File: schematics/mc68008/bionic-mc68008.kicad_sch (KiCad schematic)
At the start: 11 parts, among them J1 Bionic-P135, J2 Bionic-P245, U1 MC68008P, U2 74HCT126, U3 74HCT541, U4 74HCT541, U5 11AA010-I/TO

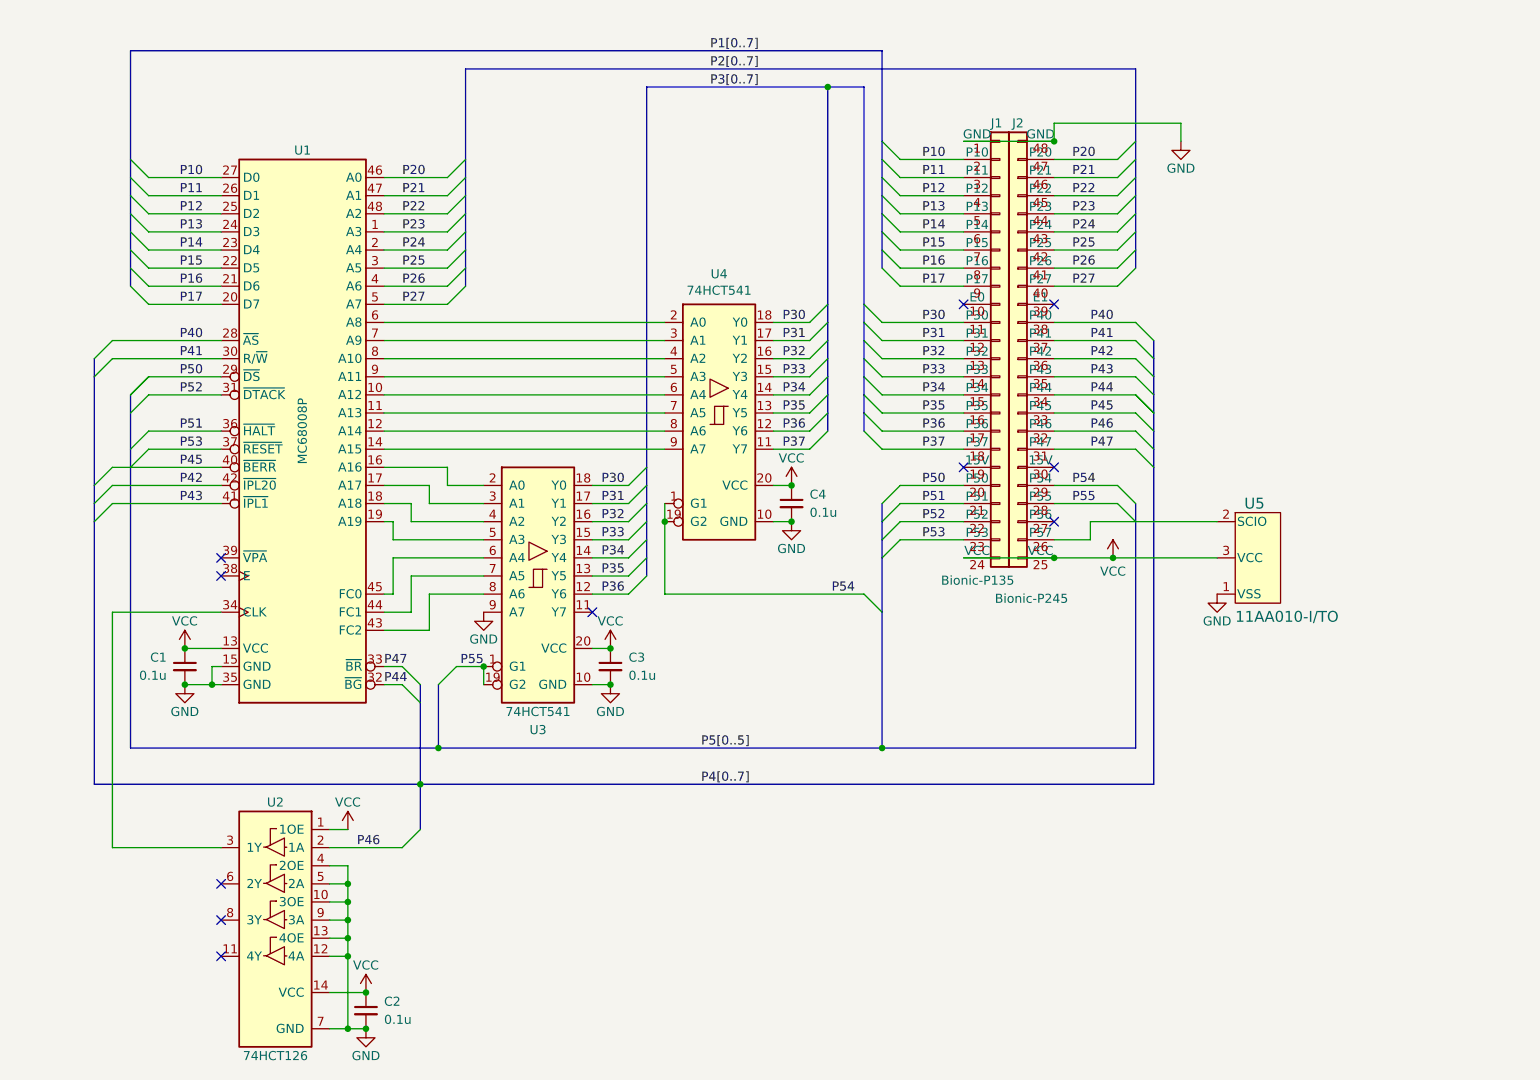
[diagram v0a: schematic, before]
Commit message: [WIP] [MC68008] Update schematics
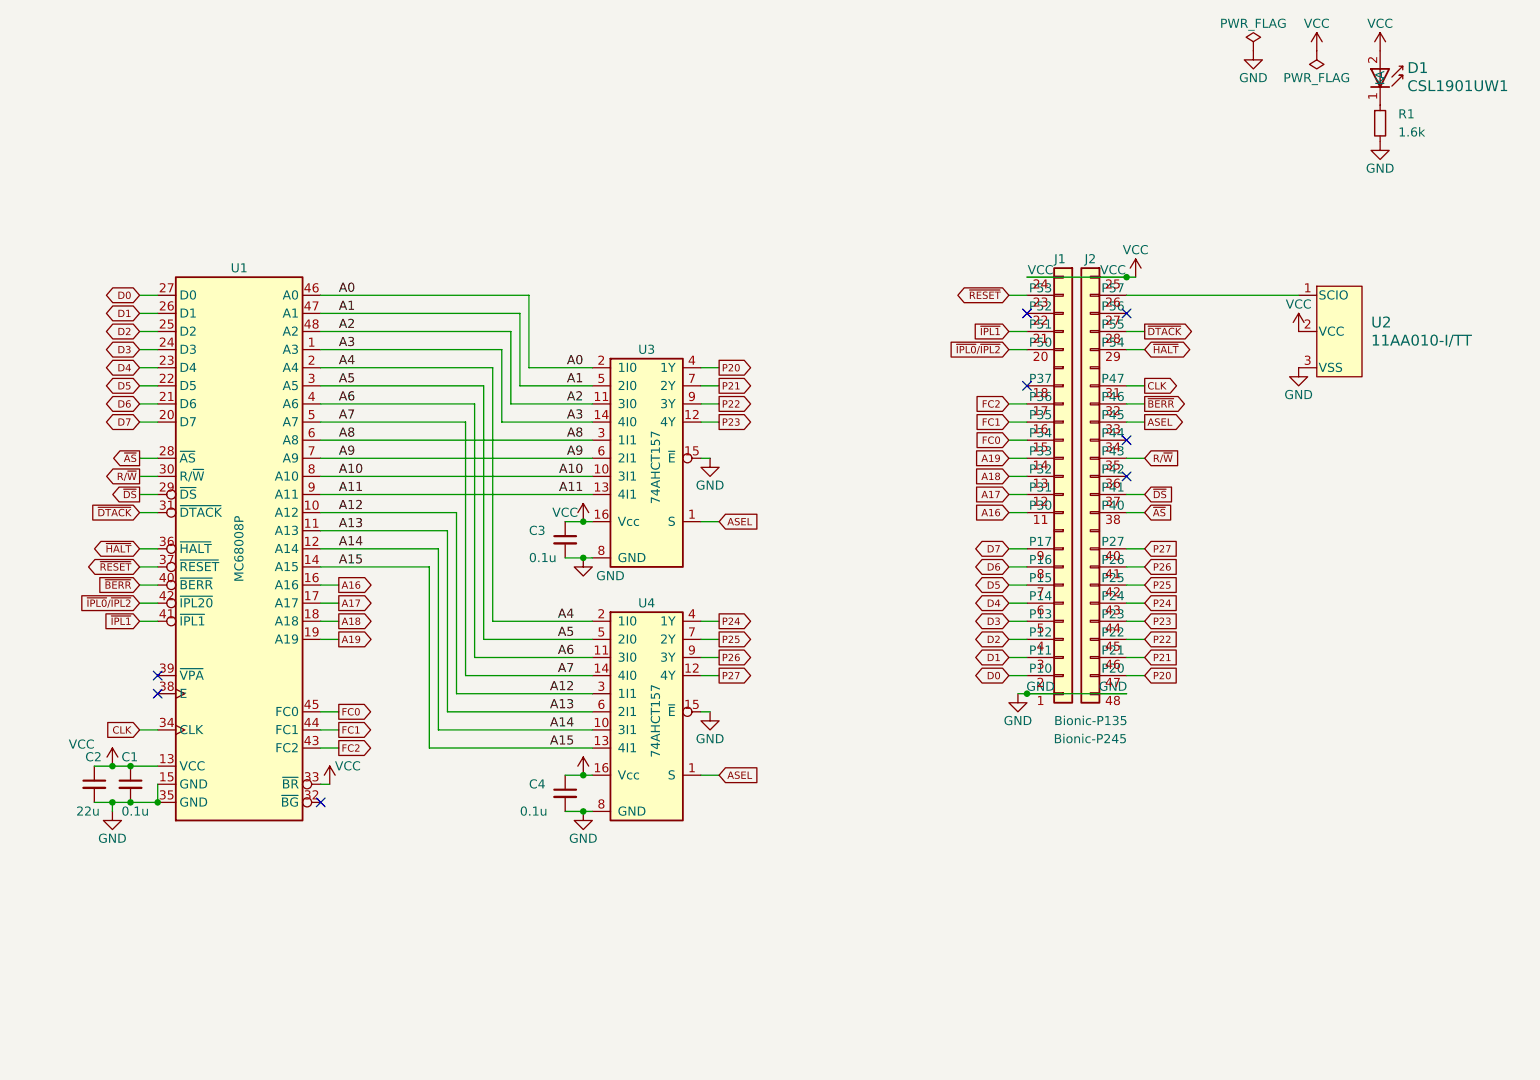
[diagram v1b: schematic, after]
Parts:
- removed J1: Bionic-P135, connector:Bionic-P135_Vertical, symbol 0-LocalLibrary:Bionic-P135
- removed J2: Bionic-P245, connector:Bionic-P245_Vertical, symbol 0-LocalLibrary:Bionic-P245
- removed U1: MC68008P, Package_DIP:DIP-48_W15.24mm, symbol 0-LocalLibrary:MC68008P
- removed U2: 74HCT126, Package_DIP:DIP-14_W7.62mm, symbol 0-LocalLibrary:74HCT126
- removed U3, U4: 74HCT541, Package_DIP:DIP-20_W7.62mm, symbol 0-LocalLibrary:74HCT541
- removed U5: 11AA010-I/TO, TO-92_MC_MCH, symbol 0-LocalLibrary:11AA010-I_TO
- added D1: CSL1901UW1, rhom:LED_CSL1901UW1_ROM-M, symbol rhom:CSL1901UW1
- added J1: Bionic-P135, bionic:Bionic-P135_SMT, symbol bionic:Bionic-P135
- added J2: Bionic-P245, bionic:Bionic-P245_SMT, symbol bionic:Bionic-P245
- added R1: 1.6k, Resistor_SMD:R_0603_1608Metric_Pad0.98x0.95mm_HandSolder, symbol Device:R_Small
- added U1: MC68008P, bionic:DIP-48_W15.24mm_Socket, symbol cpu:MC68008P
- added U2: 11AA010-I/TT, microchip:SOT-23_MC_MCH-M, symbol microchip:11AA010-I_TT
- added U3, U4: 74AHCT157, ti:PW16-M, symbol ti:74AHCT157
- C1, C3, C4: footprint Capacitor_THT:C_Disc_D3.4mm_W2.1mm_P2.50mm -> Capacitor_SMD:C_0603_1608Metric_Pad1.08x0.95mm_HandSolder
- C2: value 0.1u -> 22u; footprint Capacitor_THT:C_Disc_D3.4mm_W2.1mm_P2.50mm -> Capacitor_SMD:C_0603_1608Metric_Pad1.08x0.95mm_HandSolder
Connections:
- net GND: now also J1.1 (GND), J2.48 (GND), R1.2, U1.15 (GND), U1.35 (GND), U2.3 (VSS), U3.15 (~{E}), U3.8 (GND), U4.15 (~{E}), U4.8 (GND)
- net P20: now also J2.47 (P20), U3.4 (1Y)
- net P21: now also J2.46 (P21), U3.7 (2Y)
- net P22: now also J2.45 (P22), U3.9 (3Y)
- net P23: now also J2.44 (P23), U3.12 (4Y)
- net P24: now also J2.43 (P24), U4.4 (1Y)
- net P25: now also J2.42 (P25), U4.7 (2Y)
- net P26: now also J2.41 (P26), U4.9 (3Y)
- net P27: now also J2.40 (P27), U4.12 (4Y)
- net VCC: now also D1.2 (A), J1.24 (VCC), J2.25 (VCC), U1.13 (VCC), U1.33 (~{BR}), U2.2 (VCC), U3.16 (Vcc), U4.16 (Vcc)
- new net: J2.26 (P57), U2.1 (SCIO)
- new net: D1.1 (K), R1.1
- new net A0: U1.46 (A0), U3.2 (1I0)
- new net A1: U1.47 (A1), U3.5 (2I0)
- new net A10: U1.8 (A10), U3.10 (3I1)
- new net A11: U1.9 (A11), U3.13 (4I1)
- new net A12: U1.10 (A12), U4.3 (1I1)
- new net A13: U1.11 (A13), U4.6 (2I1)
- new net A14: U1.12 (A14), U4.10 (3I1)
- new net A15: U1.14 (A15), U4.13 (4I1)
- new net A16: J1.11 (P30), U1.16 (A16)
- new net A17: J1.12 (P31), U1.17 (A17)
- new net A18: J1.13 (P32), U1.18 (A18)
- new net A19: J1.14 (P33), U1.19 (A19)
- new net A2: U1.48 (A2), U3.11 (3I0)
- new net A3: U1.1 (A3), U3.14 (4I0)
- new net A4: U1.2 (A4), U4.2 (1I0)
- new net A5: U1.3 (A5), U4.5 (2I0)
- new net A6: U1.4 (A6), U4.11 (3I0)
- new net A7: U1.5 (A7), U4.14 (4I0)
- new net A8: U1.6 (A8), U3.3 (1I1)
- new net A9: U1.7 (A9), U3.6 (2I1)
- new net ASEL: J2.33 (P45), U3.1 (S), U4.1 (S)
- new net CLK: J2.31 (P47), U1.34 (CLK)
- new net D0: J1.2 (P10), U1.27 (D0)
- new net D1: J1.3 (P11), U1.26 (D1)
- new net D2: J1.4 (P12), U1.25 (D2)
- new net D3: J1.5 (P13), U1.24 (D3)
- new net D4: J1.6 (P14), U1.23 (D4)
- new net D5: J1.7 (P15), U1.22 (D5)
- new net D6: J1.8 (P16), U1.21 (D6)
- new net D7: J1.9 (P17), U1.20 (D7)
- new net FC0: J1.15 (P34), U1.45 (FC0)
- new net FC1: J1.16 (P35), U1.44 (FC1)
- new net FC2: J1.17 (P36), U1.43 (FC2)
- new net R/~{W}: J2.35 (P43), U1.30 (R/~{W})
- new net ~{AS}: J2.38 (P40), U1.28 (~{AS})
- new net ~{BERR}: J2.32 (P46), U1.40 (~{BERR})
- new net ~{DS}: J2.37 (P41), U1.29 (~{DS})
- new net ~{DTACK}: J2.28 (P55), U1.31 (~{DTACK})
- new net ~{HALT}: J2.29 (P54), U1.36 (~{HALT})
- new net ~{IPL0}/~{IPL2}: J1.20 (P50), U1.42 (~{IPL20})
- new net ~{IPL1}: J1.21 (P51), U1.41 (~{IPL1})
- new net ~{RESET}: J1.23 (P53), U1.37 (~{RESET})
- no-connect marks 11 -> 8
